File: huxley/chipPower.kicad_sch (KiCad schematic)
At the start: 23 parts, among them J1 CT3151V1-2, J2 CT3151V1-2, J3 CT3151V1-2, J34 CT3151V1-0, J35 CT3151V1-2, J37 CT3151V1-0

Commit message: fixed all bad refs; replaced analog discovery connector; change level shifter 3v3 to from analog discovery
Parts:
- J1, J2, J3, J34, J35, J37: footprint 726_footprints:banana_plug_CT3151V1-0 -> 0_726_footprints:banana_plug_CT3151V1-0; symbol _PHASE:CT3151V1-0 -> 0_PHASE:CT3151V1-0
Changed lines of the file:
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@@
 	)
 	(symbol
-		(lib_id "_PHASE:CT3151V1-0")
+		(lib_id "0_PHASE:CT3151V1-0")
 		(at 41.91 120.65 0)
 		(unit 1)
@@
 			)
 		)
-		(property "Footprint" "726_footprints:banana_plug_CT3151V1-0"
+		(property "Footprint" "0_726_footprints:banana_plug_CT3151V1-0"
 			(at 41.91 120.65 0)
 			(effects
@@
 	)
 	(symbol
-		(lib_id "_PHASE:CT3151V1-0")
+		(lib_id "0_PHASE:CT3151V1-0")
 		(at 41.91 68.58 0)
 		(unit 1)
@@
 			)
 		)
-		(property "Footprint" "726_footprints:banana_plug_CT3151V1-0"
+		(property "Footprint" "0_726_footprints:banana_plug_CT3151V1-0"
 			(at 41.91 68.58 0)
 			(effects
@@
 			)
 		)
-		(property "Datasheet" "CT3151V1-2"
+		(property "Datasheet" "CT3151V1-0"
 			(at 41.91 68.58 0)
 			(effects
@@
 	)
 	(symbol
-		(lib_id "_PHASE:CT3151V1-0")
+		(lib_id "0_PHASE:CT3151V1-0")
 		(at 41.91 40.64 0)
 		(unit 1)
@@
 			)
 		)
-		(property "Footprint" "726_footprints:banana_plug_CT3151V1-0"
+		(property "Footprint" "0_726_footprints:banana_plug_CT3151V1-0"
 			(at 41.91 40.64 0)
 			(effects
@@
 			)
 		)
-		(property "Datasheet" "CT3151V1-2"
+		(property "Datasheet" "CT3151V1-0"
 			(at 41.91 40.64 0)
 			(effects
@@
 	)
 	(symbol
-		(lib_id "_PHASE:CT3151V1-0")
+		(lib_id "0_PHASE:CT3151V1-0")
 		(at 41.91 54.61 0)
 		(unit 1)
@@
 			)
 		)
-		(property "Footprint" "726_footprints:banana_plug_CT3151V1-0"
+		(property "Footprint" "0_726_footprints:banana_plug_CT3151V1-0"
 			(at 41.91 54.61 0)
 			(effects
@@
 			)
 		)
-		(property "Datasheet" "CT3151V1-2"
+		(property "Datasheet" "CT3151V1-0"
 			(at 41.91 54.61 0)
 			(effects
@@
 	)
 	(symbol
-		(lib_id "_PHASE:CT3151V1-0")
+		(lib_id "0_PHASE:CT3151V1-0")
 		(at 41.91 100.33 0)
 		(unit 1)
@@
 			)
 		)
-		(property "Footprint" "726_footprints:banana_plug_CT3151V1-0"
+		(property "Footprint" "0_726_footprints:banana_plug_CT3151V1-0"
 			(at 41.91 100.33 0)
 			(effects
@@
 	)
 	(symbol
-		(lib_id "_PHASE:CT3151V1-0")
+		(lib_id "0_PHASE:CT3151V1-0")
 		(at 41.91 82.55 0)
 		(unit 1)
@@
 			)
 		)
-		(property "Footprint" "726_footprints:banana_plug_CT3151V1-0"
+		(property "Footprint" "0_726_footprints:banana_plug_CT3151V1-0"
 			(at 41.91 82.55 0)
 			(effects
@@
 			)
 		)
-		(property "Datasheet" "CT3151V1-2"
+		(property "Datasheet" "CT3151V1-0"
 			(at 41.91 82.55 0)
 			(effects

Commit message: layout_1010
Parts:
- removed C24, C28, C32: 10u, Capacitor_SMD:C_0603_1608Metric, symbol pspice:C
- removed C25, C29, C33: 0.1u, Capacitor_SMD:C_0603_1608Metric, symbol pspice:C
- removed C26, C30, C34: 1n, Capacitor_SMD:C_0603_1608Metric, symbol pspice:C
- removed C27, C31, C35: 10p, Capacitor_SMD:C_0603_1608Metric, symbol pspice:C
- added C24, C28, C32: 10u, Capacitor_SMD:C_0603_1608Metric, symbol Device:C_Small
- added C25, C29, C33: 1u, Capacitor_SMD:C_0603_1608Metric, symbol Device:C_Small
- added C26, C27, C30, C31, C34, C35: 0.1u, Capacitor_SMD:C_0603_1608Metric, symbol Device:C_Small
- added C44, C46, C48, C49, C52, C53, C56, C57: 1n, Capacitor_SMD:C_0603_1608Metric, symbol Device:C_Small
- added C45, C47, C50, C51, C54, C55, C58, C59: 10p, Capacitor_SMD:C_0603_1608Metric, symbol Device:C_Small
- C20: symbol pspice:C -> Device:C_Small
- C21: value 0.1u -> 1u; symbol pspice:C -> Device:C_Small
- C22: value 1n -> 0.1u; symbol pspice:C -> Device:C_Small
- C23: value 10p -> 0.1u; symbol pspice:C -> Device:C_Small
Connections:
- net GND: now also C24.2, C25.2, C26.2, C27.2, C28.2, C29.2, C30.2, C31.2, C32.2, C33.2, C34.2, C35.2, C44.2, C45.2, C46.2, C47.2, C48.2, C49.2, C50.2, C51.2, C52.2, C53.2, C54.2, C55.2, C56.2, C57.2, C58.2, C59.2
- net PP_SYS_3V3: now also C28.1, C29.1, C30.1, C31.1, C56.1, C57.1, C58.1, C59.1
- net PP_TAVDD_1V8: now also C24.1, C25.1, C26.1, C27.1, C52.1, C53.1, C54.1, C55.1
- net PP_VDDIO_1V8: now also C32.1, C33.1, C34.1, C35.1, C48.1, C49.1, C50.1, C51.1
- net PP_VDD_0V9: now also C44.1, C45.1, C46.1, C47.1

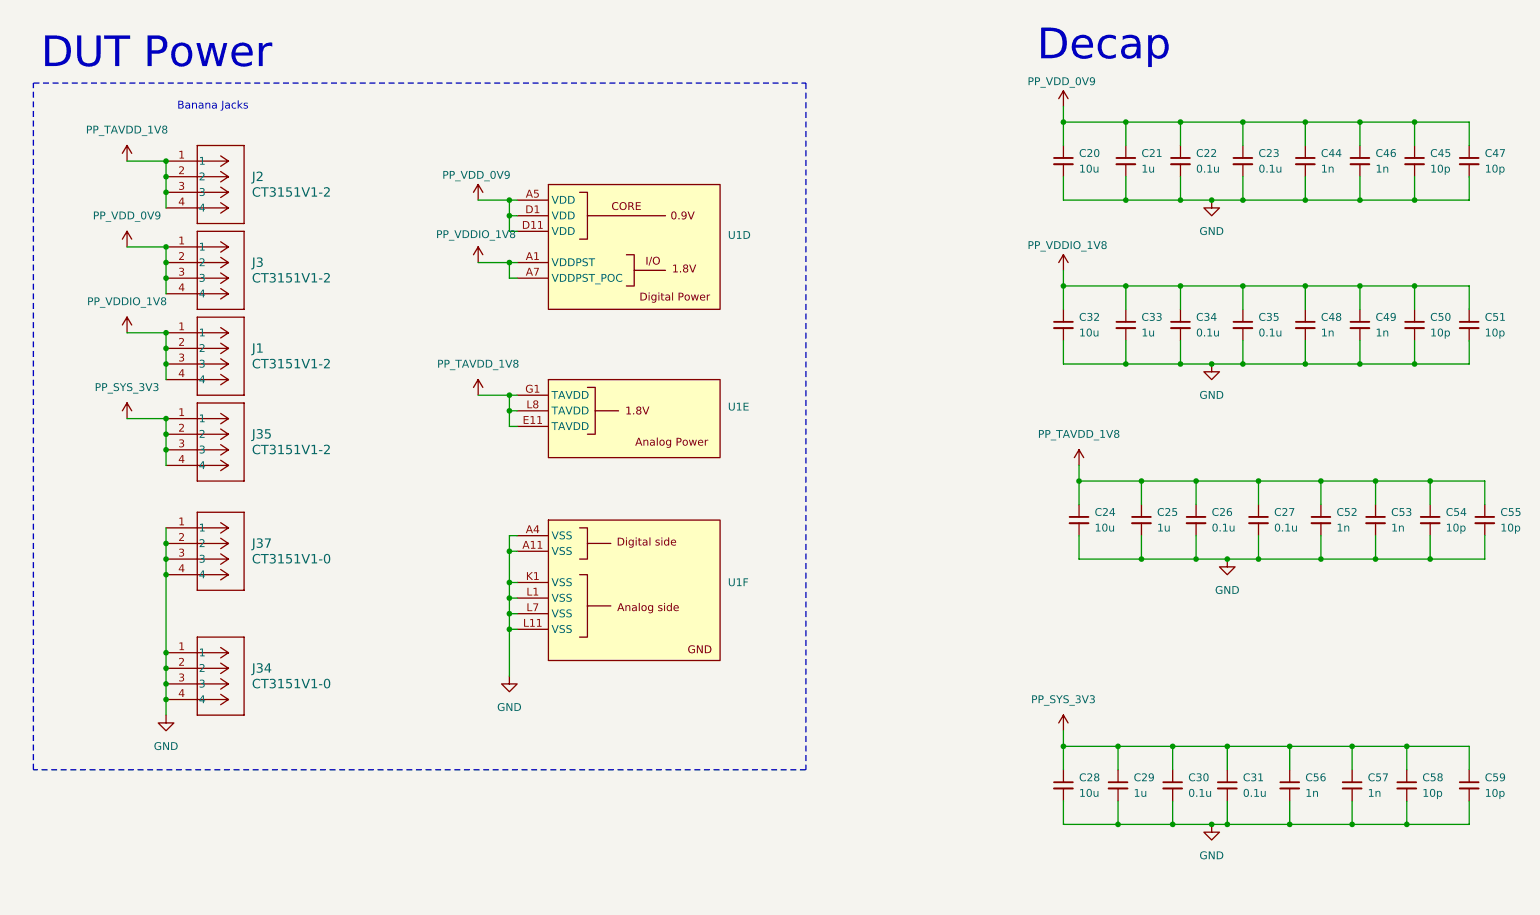
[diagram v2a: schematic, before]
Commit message: minor schematic cleanup; addition of mounting holes; minor layout adjustment
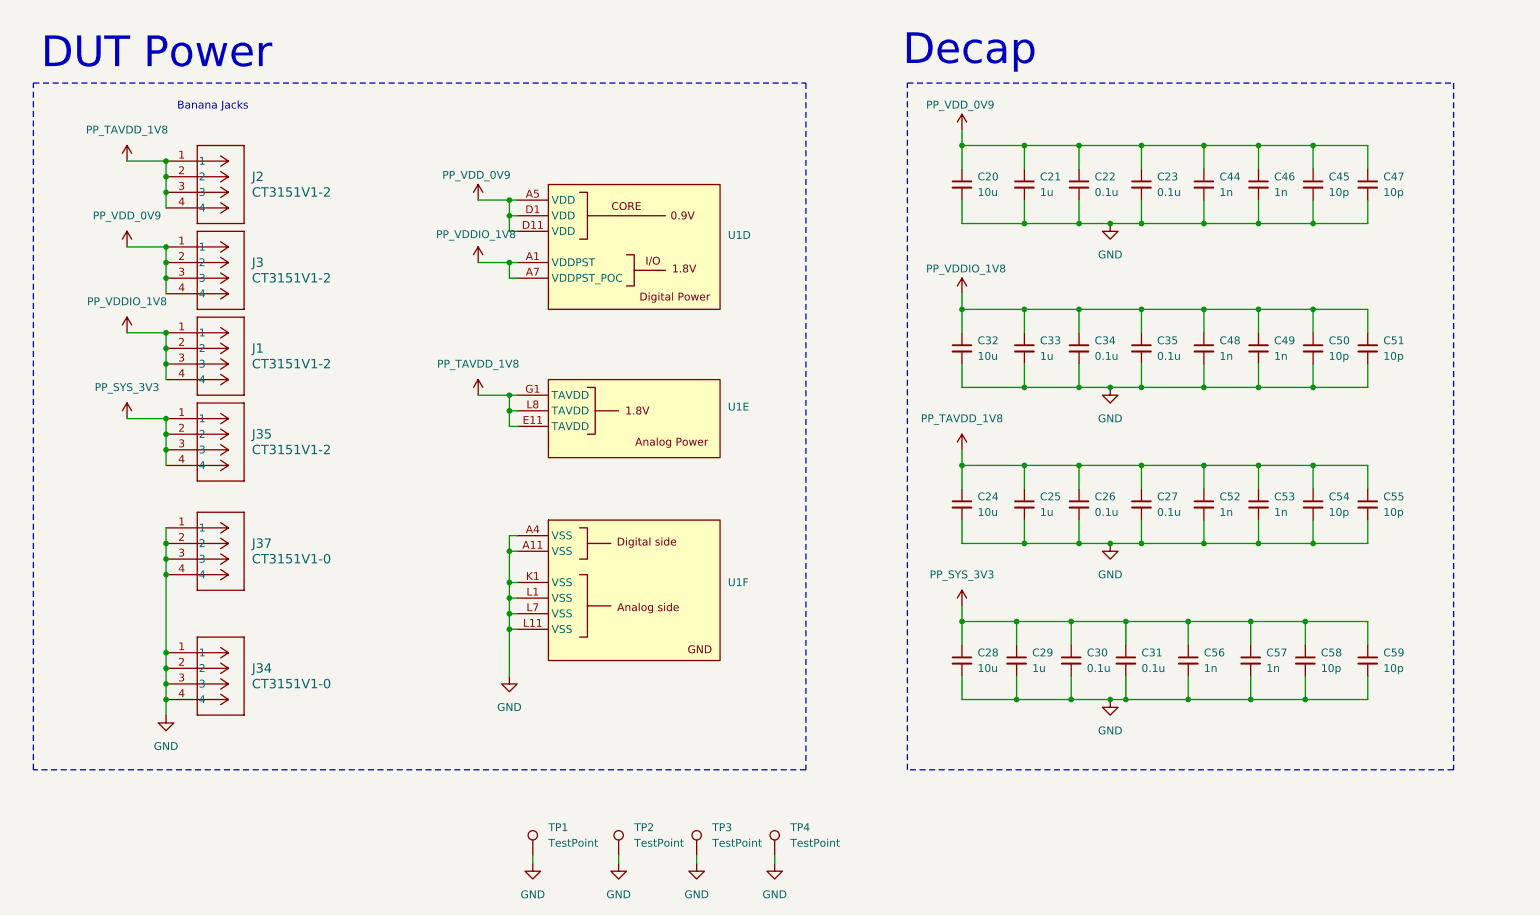
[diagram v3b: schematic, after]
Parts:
- added TP1, TP2, TP3, TP4: TestPoint, TestPoint:TestPoint_Pad_D3.0mm, symbol Connector:TestPoint
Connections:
- net GND: now also TP1.1, TP2.1, TP3.1, TP4.1
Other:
- moved on the sheet: C20, C21, C22, C23, C24, C25, C26, C27, C28, C29, C30, C31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

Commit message: pre edgechange
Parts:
- removed C56, C57: 1n, Capacitor_SMD:C_0603_1608Metric, symbol Device:C_Small
- removed C58, C59: 10p, Capacitor_SMD:C_0603_1608Metric, symbol Device:C_Small

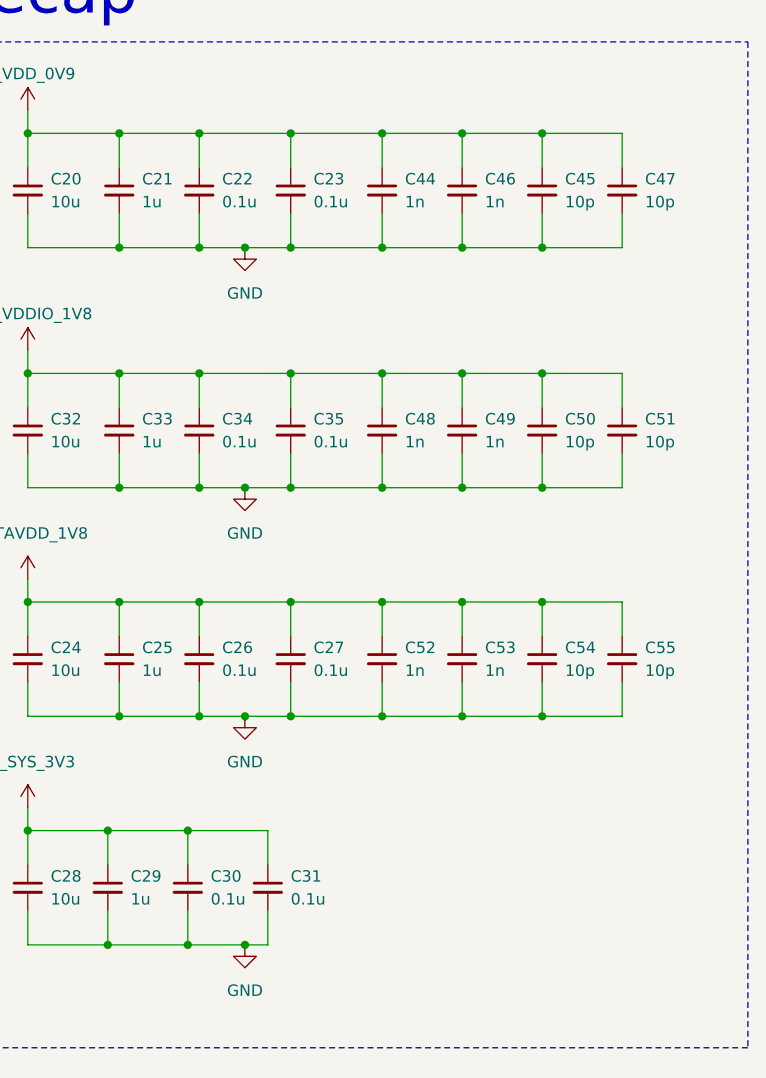
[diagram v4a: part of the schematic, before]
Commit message: added DNP prop to some caps and updated bom; added regular and rounded board outputs
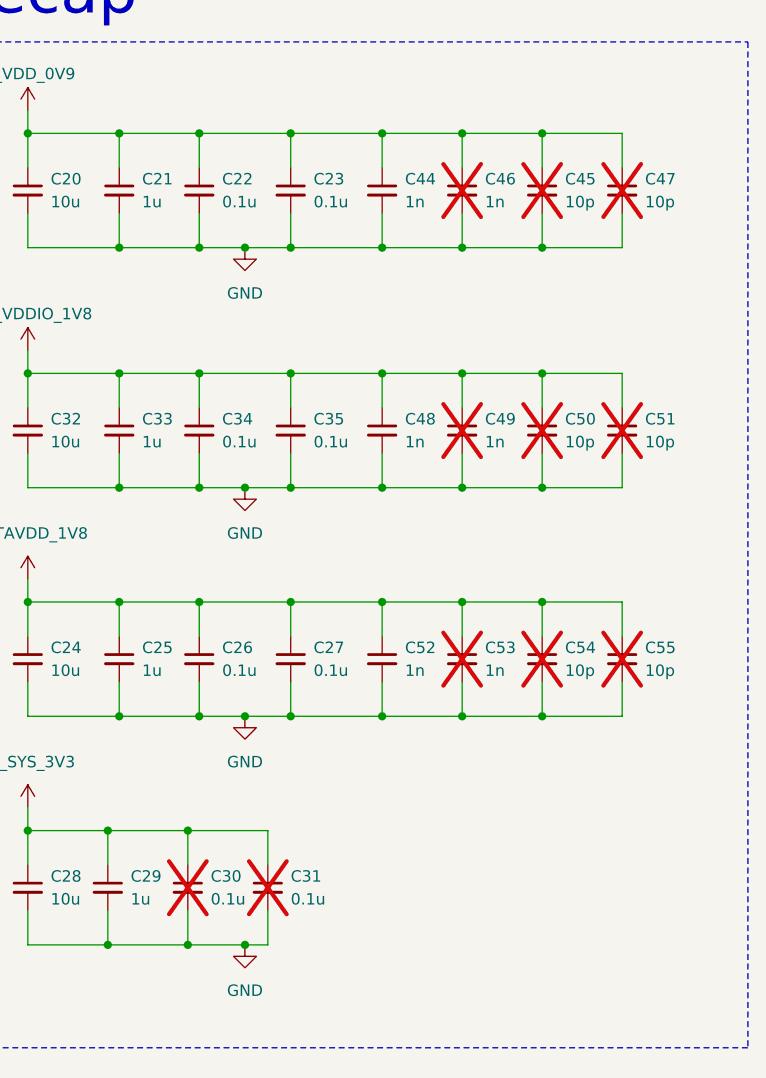
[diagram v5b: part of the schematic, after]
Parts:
- C30, C31, C45, C46, C47, C49, C50, C51, C53, C54, C55: now not fitted
- TP1, TP2, TP3, TP4: now left out of the parts list
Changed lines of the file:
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@@
 		(at 128.27 153.67 0)
 		(unit 1)
-		(exclude_from_sim no)
-		(in_bom yes)
+		(exclude_from_sim yes)
+		(in_bom no)
 		(on_board yes)
 		(dnp no)
@@
 		(in_bom yes)
 		(on_board yes)
-		(dnp no)
+		(dnp yes)
 		(fields_autoplaced yes)
 		(property "Reference" "C51"
@@
 		(at 115.57 153.67 0)
 		(unit 1)
-		(exclude_from_sim no)
-		(in_bom yes)
+		(exclude_from_sim yes)
+		(in_bom no)
 		(on_board yes)
 		(dnp no)
@@
 		(in_bom yes)
 		(on_board yes)
-		(dnp no)
+		(dnp yes)
 		(fields_autoplaced yes)
 		(property "Reference" "C49"
@@
 		(in_bom yes)
 		(on_board yes)
-		(dnp no)
+		(dnp yes)
 		(fields_autoplaced yes)
 		(property "Reference" "C50"
@@
 		(in_bom yes)
 		(on_board yes)
-		(dnp no)
+		(dnp yes)
 		(fields_autoplaced yes)
 		(property "Reference" "C45"
@@
 		(at 101.6 153.67 0)
 		(unit 1)
-		(exclude_from_sim no)
-		(in_bom yes)
+		(exclude_from_sim yes)
+		(in_bom no)
 		(on_board yes)
 		(dnp no)
@@
 		(in_bom yes)
 		(on_board yes)
-		(dnp no)
+		(dnp yes)
 		(fields_autoplaced yes)
 		(property "Reference" "C55"
@@
 		(in_bom yes)
 		(on_board yes)
-		(dnp no)
+		(dnp yes)
 		(fields_autoplaced yes)
 		(property "Reference" "C46"
@@
 		(in_bom yes)
 		(on_board yes)
-		(dnp no)
+		(dnp yes)
 		(fields_autoplaced yes)
 		(property "Reference" "C31"
@@
 		(in_bom yes)
 		(on_board yes)
-		(dnp no)
+		(dnp yes)
 		(fields_autoplaced yes)
 		(property "Reference" "C53"
@@
 		(in_bom yes)
 		(on_board yes)
-		(dnp no)
+		(dnp yes)
 		(fields_autoplaced yes)
 		(property "Reference" "C30"
@@
 		(at 140.97 153.67 0)
 		(unit 1)
-		(exclude_from_sim no)
-		(in_bom yes)
+		(exclude_from_sim yes)
+		(in_bom no)
 		(on_board yes)
 		(dnp no)
@@
 		(in_bom yes)
 		(on_board yes)
-		(dnp no)
+		(dnp yes)
 		(fields_autoplaced yes)
 		(property "Reference" "C54"
@@
 		(in_bom yes)
 		(on_board yes)
-		(dnp no)
+		(dnp yes)
 		(fields_autoplaced yes)
 		(property "Reference" "C47"
